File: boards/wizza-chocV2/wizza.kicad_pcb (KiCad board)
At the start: 2 copper layers, 106.6 x 87.7 mm, 27 parts

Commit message: wizza choc v2
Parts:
- removed the ? at (141.1, -61.4)
- removed the ? at (47.9, -58.6)
- removed the ? at (140.8, -115.2)
- removed the ? at (61.8, -117.2)
- removed B1: , kbd:ResetSW
- removed G*** (x2): LOGO, LOGO
- removed PAD1: , lib:bat
- removed REF**: Tenting Puck, Alaa:Tenting_Puck_3_Holes
- removed S17, S19, S21, S23, S27, S29, S31, S33: , Alaa:ChocV2SimpleReversible
- removed T1, T2: , E73:SPDT_C128955
- added ?: , clipboard:588d3aa5-8931-420f-9c57-a8cdf3d19d32, F.Cu at (239.9, 105.7)
- added S1: , Alaa:ChocV2hotswap, F.Cu at (212.1, 117.4)
- added S10: , Alaa:ChocV2hotswap, F.Cu at (271.1, 97.0)
- added S12: , Alaa:ChocV2hotswap, F.Cu at (290.5, 108.4)
- added S13: , Alaa:ChocV2hotswap, F.Cu at (290.5, 89.4)
- added S2: , Alaa:ChocV2hotswap, F.Cu at (206.5, 99.2)
- added S4: , Alaa:ChocV2hotswap, F.Cu at (228.8, 94.7)
- added S6: , Alaa:ChocV2hotswap, F.Cu at (250.7, 103.4)
- added S8: , Alaa:ChocV2hotswap, F.Cu at (247.4, 65.6)
- MCU1: footprint ProMicro -> Alaa:ProMicro32keys; moved to F.Cu
- S11, S15, S3, S5, S7, S9: footprint Alaa:ChocV2SimpleReversible -> Alaa:ChocV2hotswap
- S14: renamed from S13; footprint Alaa:ChocV2SimpleReversible -> Alaa:ChocV2hotswap
- moved S15 310.6 mm to (295.1, 140.7), turned to 0 degrees
- moved S9 282.9 mm to (271.1, 116.0), turned to 0 degrees
- moved S14 282.1 mm to (275.7, 139.0), turned to 0 degrees
- moved S11 271.0 mm to (271.1, 78.0), turned to 0 degrees
- moved S3 249.0 mm to (232.1, 113.4), turned to 10 degrees
- moved MCU1 237.7 mm to (212.9, 140.0)
- moved S5 234.1 mm to (225.5, 76.0), turned to 10 degrees
- moved S7 230.6 mm to (249.1, 84.5), turned to 5 degrees
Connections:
- MCU1 pad 10: P14 -> matrix_inner_bottom
- MCU1 pad 11: P16 -> thumb_tucky
- MCU1 pad 12: P10 -> thumb_reachy
- MCU1 pad 16: (no net) -> GND
- MCU1 pad 17: P2 -> matrix_pinky_top
- MCU1 pad 18: P3 -> matrix_pinky_home
- MCU1 pad 19: P4 -> matrix_ring_top
- MCU1 pad 20: P5 -> matrix_ring_home
- MCU1 pad 21: P6 -> matrix_ring_bottom
- MCU1 pad 22: P7 -> matrix_middle_top
- MCU1 pad 23: P8 -> matrix_middle_home
- MCU1 pad 24: P9 -> matrix_middle_bottom
- MCU1 pad 4: (no net) -> VCC
- MCU1 pad 5: P21 -> (no net)
- MCU1 pad 6: P20 -> matrix_index_top
- MCU1 pad 7: P19 -> matrix_index_home
- MCU1 pad 8: P18 -> matrix_index_bottom
- MCU1 pad 9: P15 -> matrix_inner_home
- S11 pad 1: P19 -> GND
- S11 pad 2: GND -> matrix_index_top
- S14 pad 1: P10 -> GND
- S14 pad 2: GND -> thumb_tucky
- S15 pad 1: P16 -> GND
- S15 pad 2: GND -> thumb_reachy
- S3 pad 1: P21 -> GND
- S3 pad 2: GND -> matrix_ring_bottom
- S5 pad 1: P20 -> GND
- S5 pad 2: GND -> matrix_ring_top
- S7 pad 1: P15 -> GND
- S7 pad 2: GND -> matrix_middle_home
- S9 pad 1: P18 -> GND
- S9 pad 2: GND -> matrix_index_bottom
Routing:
- net matrix_inner_home: track 0.00 -> 149.2 mm
- net matrix_index_top: track 0.00 -> 148.9 mm
- net matrix_inner_bottom: track 0.00 -> 128.2 mm
- net matrix_index_home: track 0.00 -> 127.4 mm
- net matrix_middle_top: track 0.00 -> 115.6 mm
- net P3: track 109.4 -> 0.00 mm
- net P6: track 108.6 -> 0.00 mm
- net matrix_index_bottom: track 0.00 -> 106.1 mm
- net thumb_reachy: track 0.00 -> 100.0 mm
- net matrix_middle_home: track 0.00 -> 89.6 mm
- net P4: track 89.3 -> 0.00 mm
- net P7: track 88.2 -> 0.00 mm
- net matrix_ring_top: track 0.00 -> 87.0 mm
- net RAW: track 93.6 -> 7.75 mm, vias 2 -> 1
- net thumb_tucky: track 0.00 -> 81.8 mm
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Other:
- board size 106.6 x 87.7 mm -> 110.2 x 92.6 mm

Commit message: wizza choc v2
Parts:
- added ?: , , F.Cu at (200.7, 124.5)
- added ?: , , F.Cu at (297.7, 62.5)
- added ?: , , F.Cu at (216.9, 62.5)
- added ?: , , F.Cu at (298.2, 124.7)
- added B1: , kbd:ResetSW, F.Cu at (233.2, 134.7)
- added PAD1: , lib:bat, F.Cu at (202.5, 71.4)
- added T1, T2: , E73:SPDT_C128955, F.Cu at (205.0, 59.1)
- moved MCU1 2.00 mm to (212.9, 138.0)
- moved S14 2.00 mm to (275.7, 137.0)
- moved S15 2.00 mm to (295.1, 138.7)
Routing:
- net RAW: track 7.75 -> 94.9 mm, vias 1 -> 2
- net b+: track 0.00 -> 45.0 mm
- net RST: track 7.75 -> 37.0 mm
- net matrix_inner_home: track 149.2 -> 146.9 mm
- net matrix_inner_bottom: track 128.2 -> 126.0 mm
- net matrix_index_top: track 148.9 -> 146.9 mm
- net matrix_index_bottom: track 106.1 -> 104.3 mm
- net matrix_index_home: track 127.4 -> 125.6 mm
- net matrix_ring_bottom: track 53.1 -> 51.9 mm
- net matrix_middle_top: track 115.6 -> 114.3 mm
- net matrix_middle_bottom: track 74.8 -> 73.6 mm
- net matrix_middle_home: track 89.6 -> 88.4 mm
- net thumb_reachy: track 100.0 -> 99.0 mm
- net matrix_pinky_home: track 38.9 -> 37.9 mm
- net matrix_ring_top: track 87.0 -> 86.0 mm
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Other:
- board size 110.2 x 92.6 mm -> 110.2 x 90.6 mm

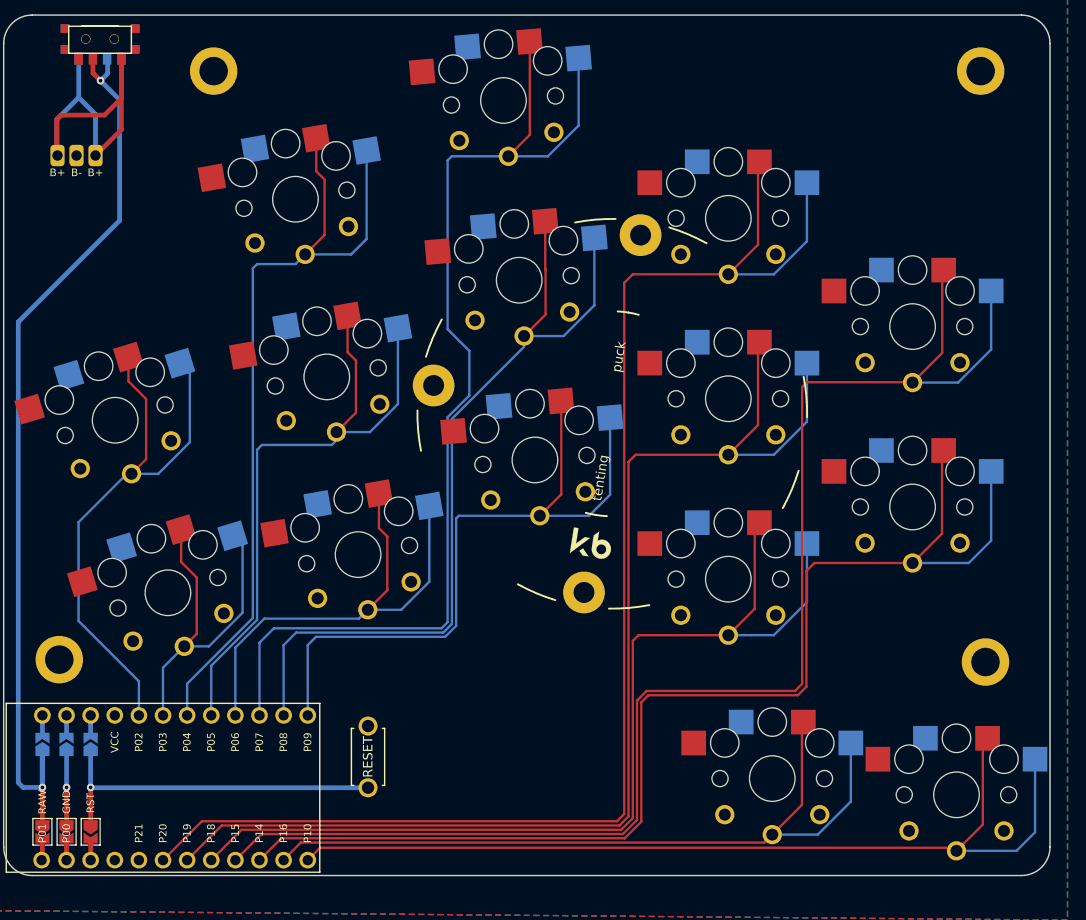
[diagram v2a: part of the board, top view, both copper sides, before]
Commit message: basbousa new case with holes and chocV2 change
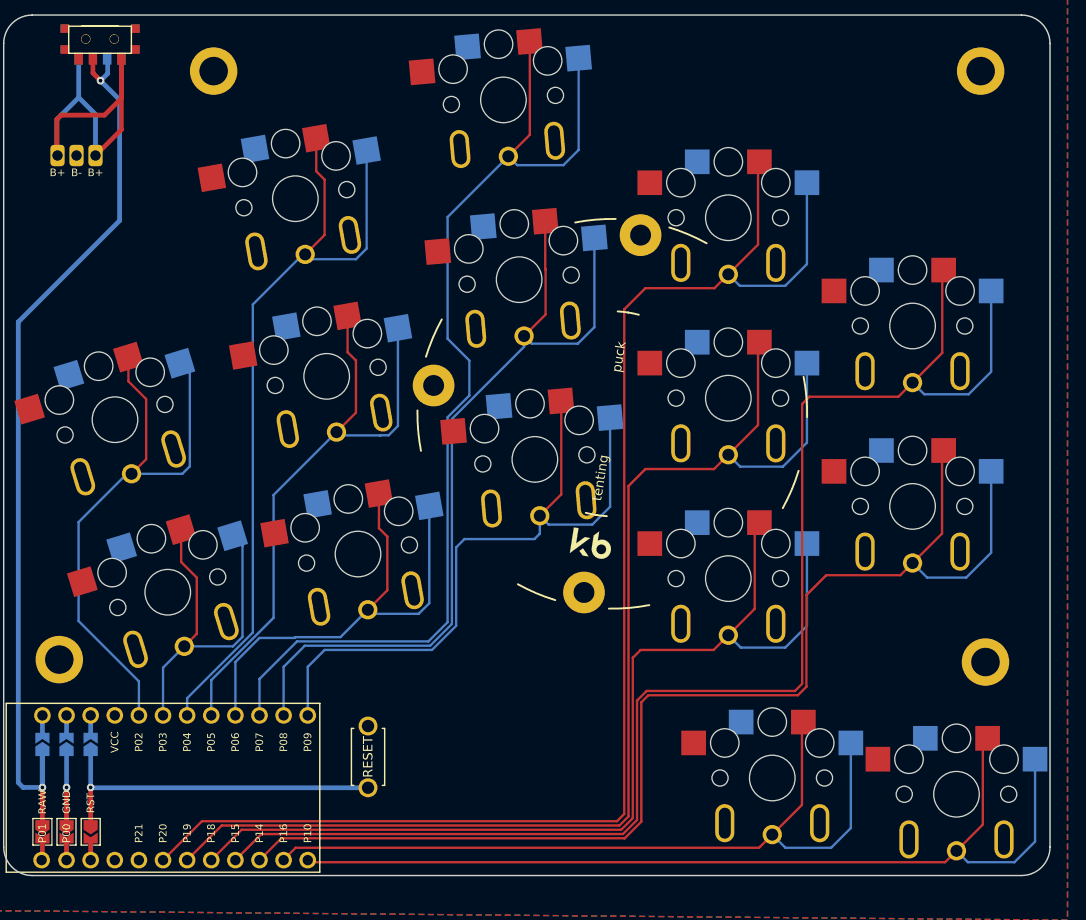
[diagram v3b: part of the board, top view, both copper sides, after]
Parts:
- S1, S10, S11, S12, S13, S14, S15, S2, S3, S4, S5, S6, S7, S8, S9: footprint Alaa:ChocV2hotswap -> Alaa:ChocV2hotswapWithSupportOval
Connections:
- S1 pad : matrix_pinky_home -> (no net)
- S2 pad : matrix_pinky_top -> (no net)
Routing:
- net matrix_middle_top: track 114.3 -> 110.9 mm
- net thumb_tucky: track 81.5 -> 84.3 mm
- net matrix_ring_home: track 68.8 -> 66.1 mm
- net matrix_index_bottom: track 104.3 -> 105.8 mm
- net matrix_pinky_top: track 60.6 -> 62.1 mm
- net thumb_reachy: track 99.0 -> 100.5 mm
- net matrix_pinky_home: track 37.9 -> 39.3 mm
- net matrix_inner_home: track 146.9 -> 148.3 mm
- net matrix_ring_top: track 86.0 -> 84.8 mm
- net matrix_index_home: track 125.6 -> 126.5 mm
- net matrix_ring_bottom: track 51.9 -> 52.7 mm
- net matrix_index_top: track 146.9 -> 147.7 mm
- net matrix_middle_home: track 88.4 -> 89.1 mm
- net matrix_inner_bottom: track 126.0 -> 126.5 mm
- net matrix_middle_bottom: track 73.6 -> 73.1 mm
